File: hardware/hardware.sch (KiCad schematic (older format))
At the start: 76 parts, among them J1 DB25_Female, J2 USB_B_Micro, J3 RJ45_Bel_SI-60062-F-68net, J4 Conn_02x06_Odd_Even, U1 LD1117S33TR_SOT223, U11 ENC28J60x-SO, U12 74HC14, U2 74LS126, U3 74LS126, U4 LM1117-ADJ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

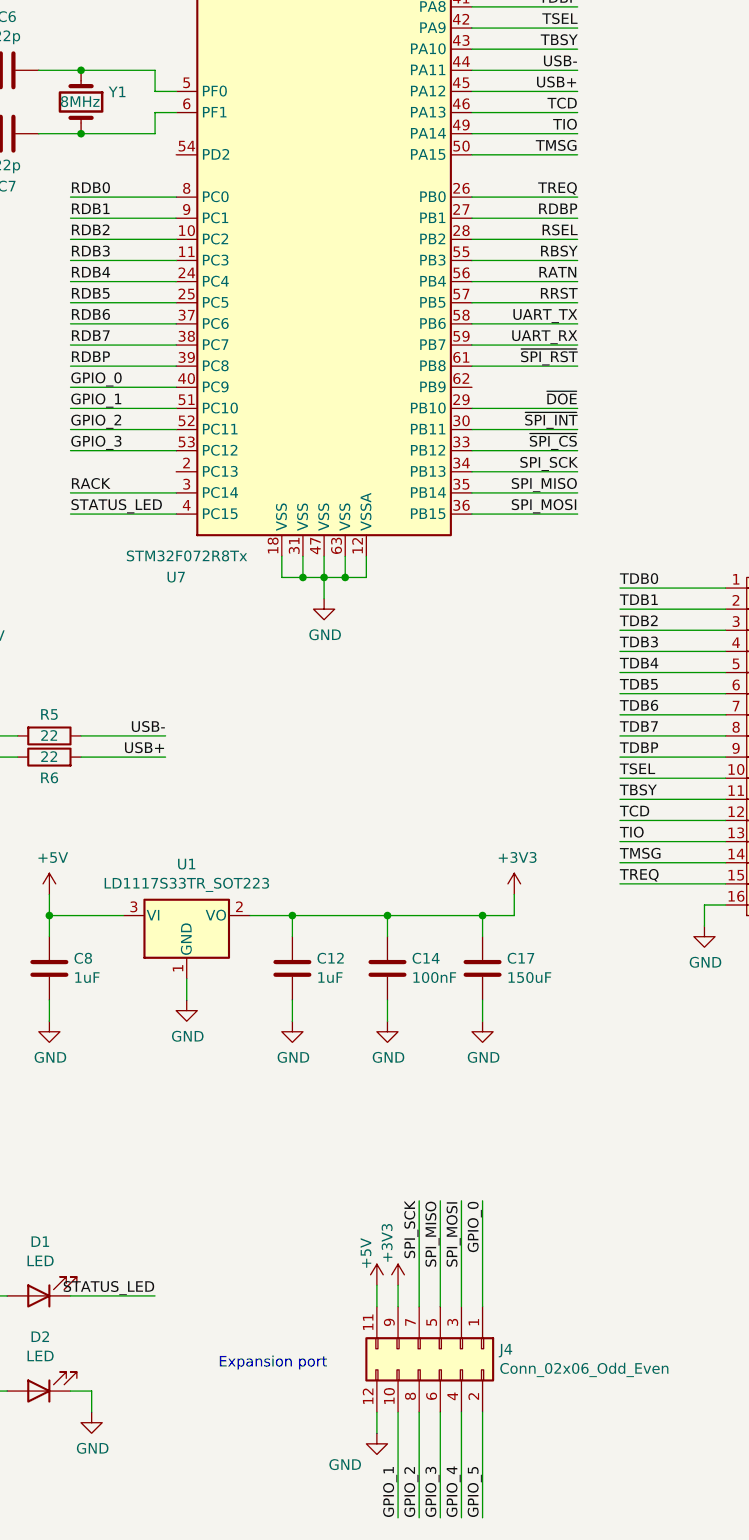
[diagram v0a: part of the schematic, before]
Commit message: fix: drc and unused pins
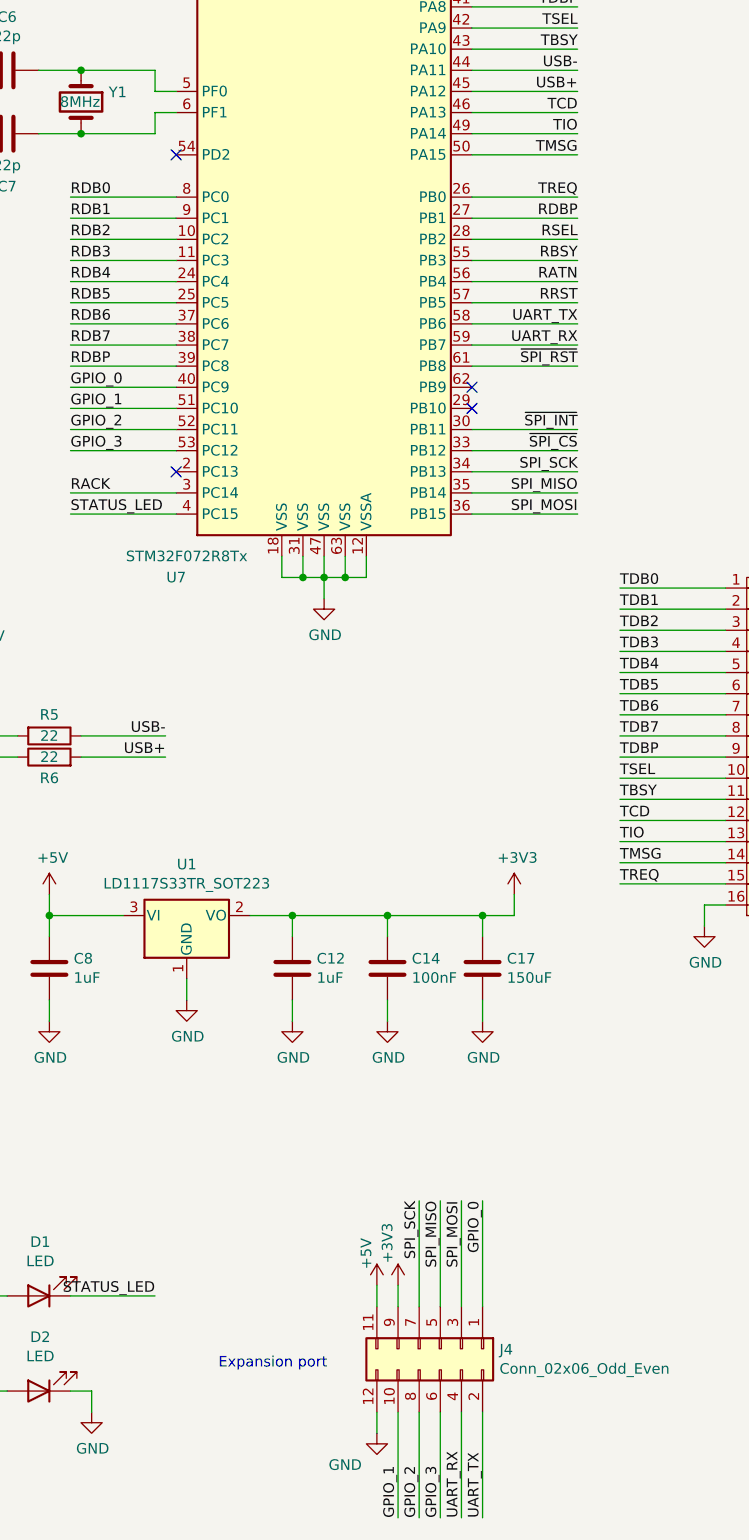
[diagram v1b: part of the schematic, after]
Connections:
- net GPIO_4 is gone; now on net UART_RX: J4.4 (Pin_4)
- net GPIO_5 is gone; now on net UART_TX: J4.2 (Pin_2)
- net ~DOE~: no longer names the net of U7.29 (PB10)
- no-connect marks 10 -> 14
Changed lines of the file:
@@
 Text Label 6200 6850 0    50   ~ 0
 RDB0
-Text Label 4200 5700 2    50   ~ 0
-~DOE~
 $Comp
 L power:+3V3 #PWR040
@@
 UART_TX
 Text Label 3750 10950 1    50   ~ 0
-GPIO_5
+UART_TX
 Text Label 3650 10950 1    50   ~ 0
-GPIO_4
-Wire Wire Line
-	3700 5700 4200 5700
+UART_RX
+NoConn ~ 2300 6000
+NoConn ~ 3700 5600
+NoConn ~ 3700 5700
+NoConn ~ 2300 4500
 $EndSCHEMATC
